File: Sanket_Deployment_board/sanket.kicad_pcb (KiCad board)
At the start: 2 copper layers, 95.9 x 92 mm, 42 parts, among them J2 Conn_02x03_Counter_Clockwise, J3 Conn_02x03_Counter_Clockwise, U1 SN74LVC1G17QDCKRQ1

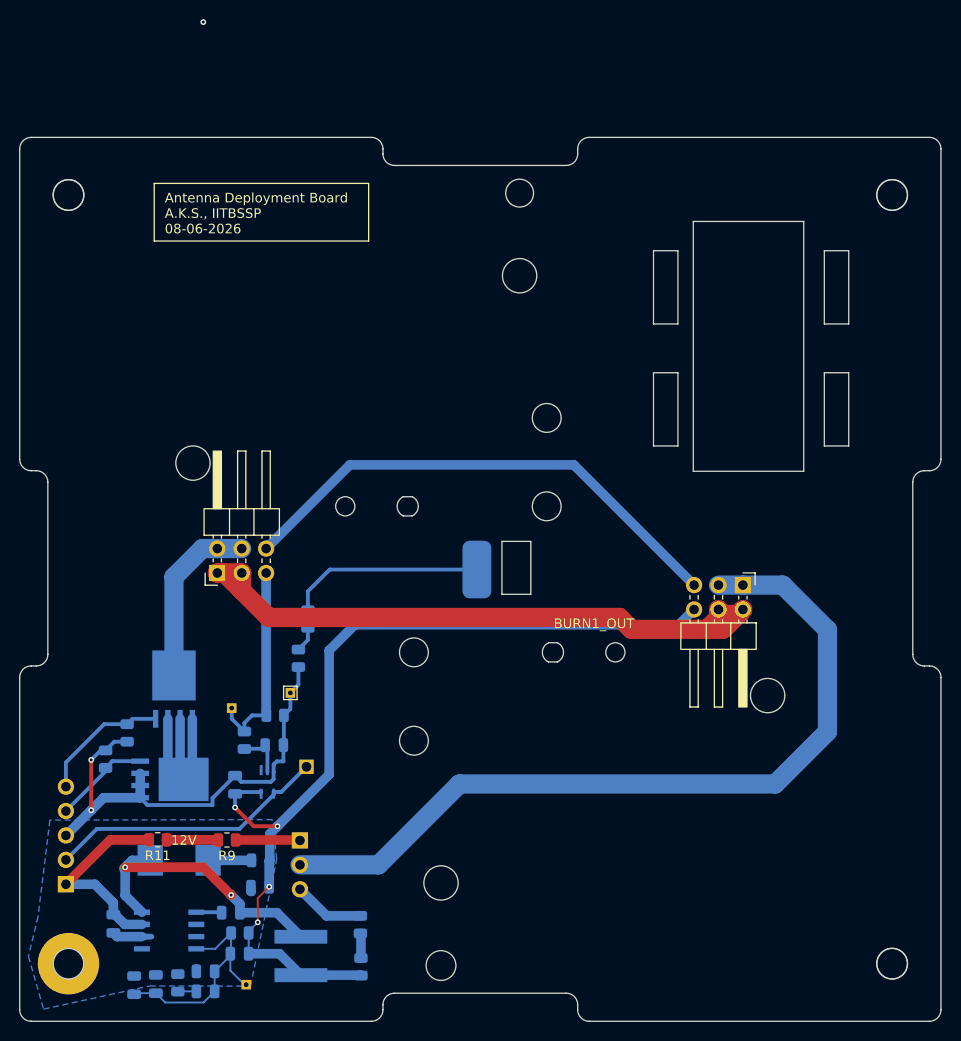
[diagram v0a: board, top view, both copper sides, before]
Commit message: Aligned holes according to PC104, flipped header used to choose burn power, corrected silkscreen
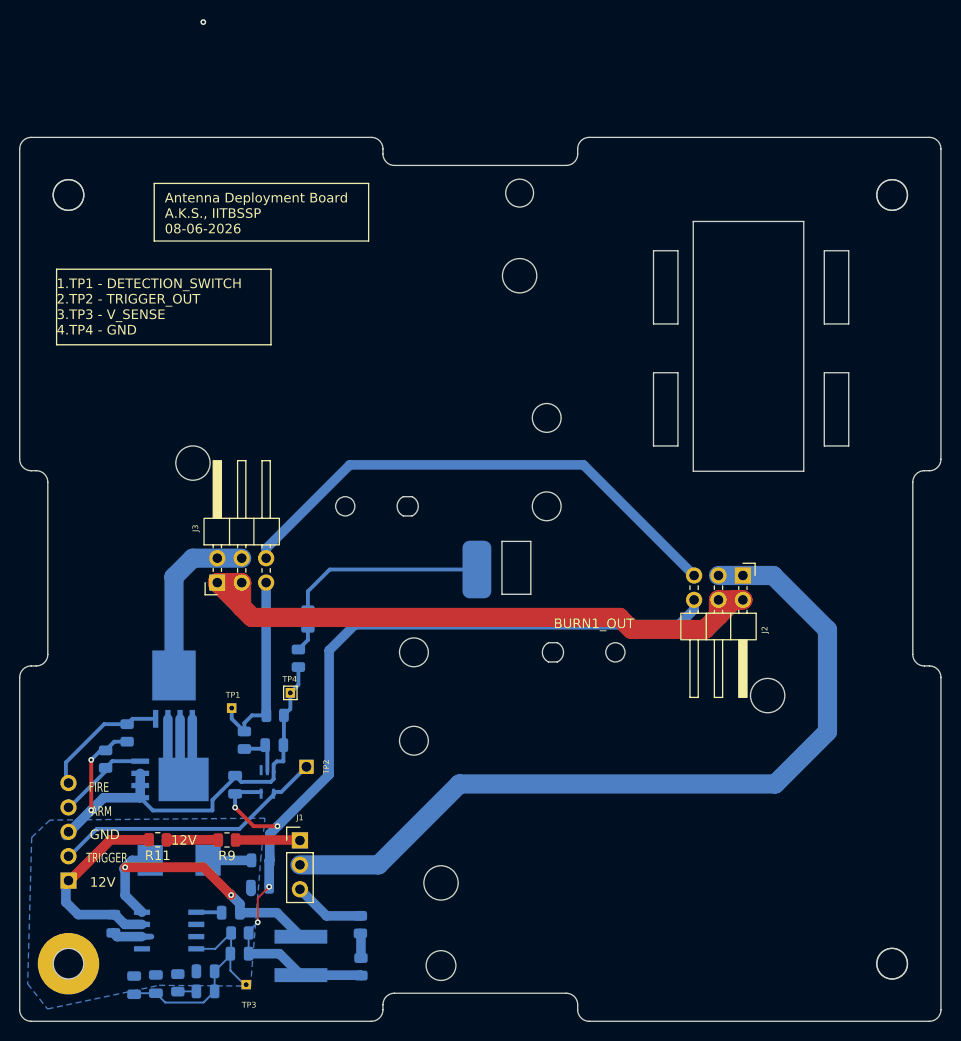
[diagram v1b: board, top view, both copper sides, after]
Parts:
- J1: moved to F.Cu
- moved J2 1.00 mm to (175.8, 102.9)
- moved J3 1.00 mm to (121.1, 103.6)
- moved J8 0.47 mm to (105.6, 134.7)
- turned J1 to 0 degrees
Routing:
- net /BurnWire1OUT: track 67.4 -> 68.8 mm
- net /DeployerDetectionSW2OUT: track 21.3 -> 20.3 mm
- net +3V3: track 96.5 -> 97.5 mm
- net GND: track 61.9 -> 62.7 mm
- net /NMOS_DRAIN: track 18.8 -> 18.1 mm
- net /DeployerDetectionSW1OUT: track 53.3 -> 53.9 mm
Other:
- board text added: "1.TP1 - DETECTION_SWITCH 2.TP2 - TRIGGER_OUT 3.TP3 - V_SENSE 4.TP4 - GND"

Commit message: Added step file for ADS_V8
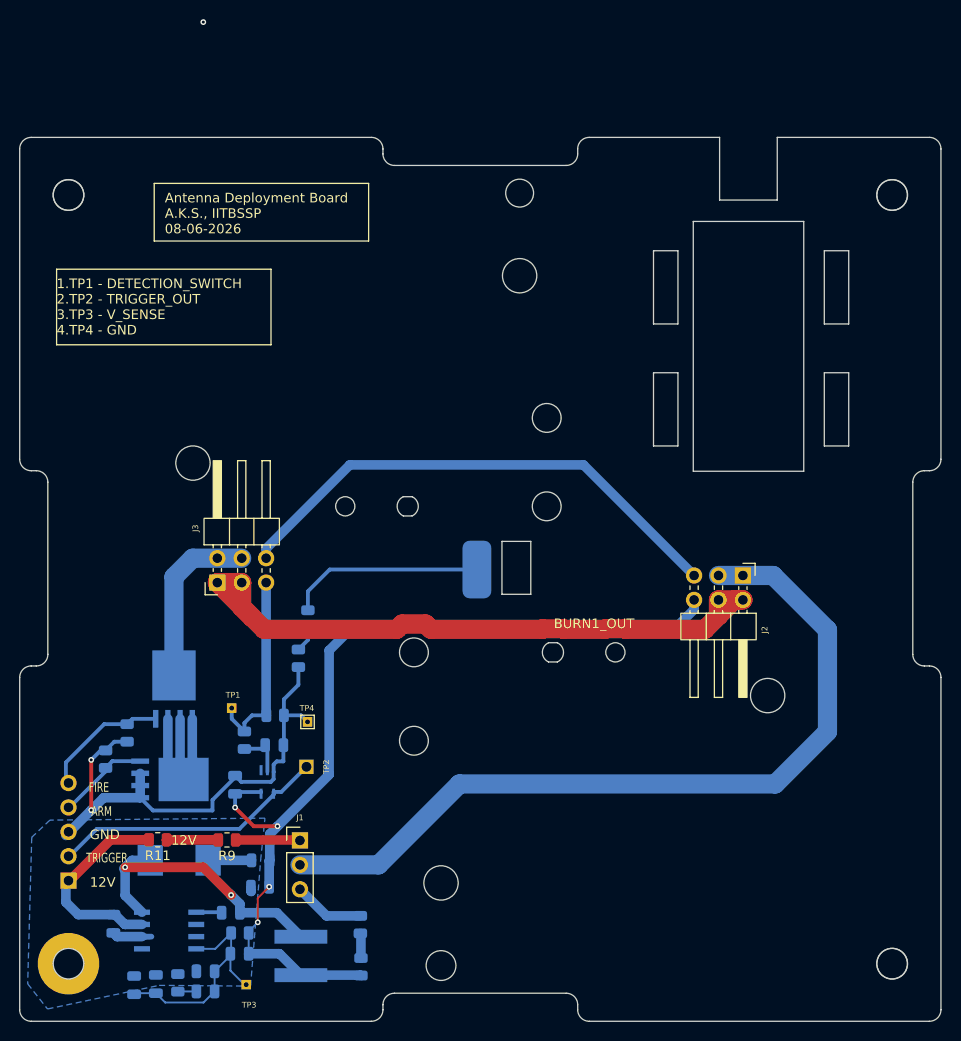
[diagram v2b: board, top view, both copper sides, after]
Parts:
- moved TP4 3.51 mm to (130.5, 118.1)
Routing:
- net GND: track 62.7 -> 65.4 mm
- net /BurnWire1OUT: track 68.8 -> 69.3 mm
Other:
- outline, holes or cut-outs redrawn
